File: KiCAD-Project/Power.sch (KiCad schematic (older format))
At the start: 19 parts, among them U401 DRV8323SRTAR-DRV8323SRTAR

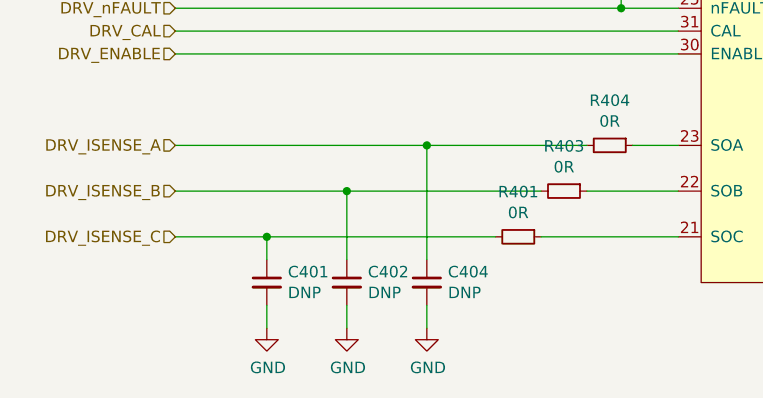
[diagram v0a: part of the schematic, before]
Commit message: Schamtic package assigned
Package assigned, added two 100nF C's for temp sensors
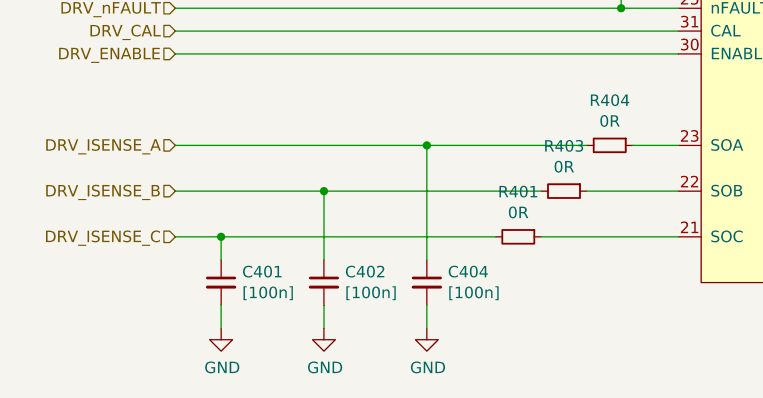
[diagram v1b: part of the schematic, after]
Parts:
- C401, C402, C404: value DNP -> [100n]; footprint (none) -> Capacitor_SMD:C_0603_1608Metric
- C403: footprint (none) -> Capacitor_SMD:C_1206_3216Metric
- C405, C406, C407, C408, C409: footprint (none) -> Capacitor_SMD:C_0603_1608Metric
- R401, R402, R403, R404, R405: footprint (none) -> Resistor_SMD:R_0603_1608Metric
- TP401, TP402, TP403, TP404: footprint (none) -> TestPoint:TestPoint_Pad_D2.0mm
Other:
- moved on the sheet: C401, C402
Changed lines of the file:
@@
 F 0 "R405" H 5009 4096 50  0000 L CNN
 F 1 "10k" H 5009 4005 50  0000 L CNN
-F 2 "" H 4950 4050 50  0001 C CNN
+F 2 "Resistor_SMD:R_0603_1608Metric" H 4950 4050 50  0001 C CNN
 F 3 "~" H 4950 4050 50  0001 C CNN
 	1    4950 4050
@@
 F 0 "R402" H 4709 4096 50  0000 L CNN
 F 1 "10k" H 4709 4005 50  0000 L CNN
-F 2 "" H 4650 4050 50  0001 C CNN
+F 2 "Resistor_SMD:R_0603_1608Metric" H 4650 4050 50  0001 C CNN
 F 3 "~" H 4650 4050 50  0001 C CNN
 	1    4650 4050
@@
 F 0 "R404" V 4704 5200 50  0000 C CNN
 F 1 "0R" V 4795 5200 50  0000 C CNN
-F 2 "" H 4900 5200 50  0001 C CNN
+F 2 "Resistor_SMD:R_0603_1608Metric" H 4900 5200 50  0001 C CNN
 F 3 "~" H 4900 5200 50  0001 C CNN
 	1    4900 5200
@@
 F 0 "R403" V 4504 5400 50  0000 C CNN
 F 1 "0R" V 4595 5400 50  0000 C CNN
-F 2 "" H 4700 5400 50  0001 C CNN
+F 2 "Resistor_SMD:R_0603_1608Metric" H 4700 5400 50  0001 C CNN
 F 3 "~" H 4700 5400 50  0001 C CNN
 	1    4700 5400
@@
 F 0 "R401" V 4304 5600 50  0000 C CNN
 F 1 "0R" V 4395 5600 50  0000 C CNN
-F 2 "" H 4500 5600 50  0001 C CNN
+F 2 "Resistor_SMD:R_0603_1608Metric" H 4500 5600 50  0001 C CNN
 F 3 "~" H 4500 5600 50  0001 C CNN
 	1    4500 5600
@@
 AR Path="/60AFCC9B/60B2332E" Ref="C404"  Part="1"
 F 0 "C404" H 4192 5846 50  0000 L CNN
-F 1 "DNP" H 4192 5755 50  0000 L CNN
-F 2 "" H 4100 5800 50  0001 C CNN
+F 1 "[100n]" H 4192 5755 50  0000 L CNN
+F 2 "Capacitor_SMD:C_0603_1608Metric" H 4100 5800 50  0001 C CNN
 F 3 "~" H 4100 5800 50  0001 C CNN
 	1    4100 5800
@@
 F 0 "TP403" H 3858 4218 50  0000 L CNN
 F 1 "SPI_SCK" H 3858 4127 50  0000 L CNN
-F 2 "" H 4000 4100 50  0001 C CNN
+F 2 "TestPoint:TestPoint_Pad_D2.0mm" H 4000 4100 50  0001 C CNN
 F 3 "~" H 4000 4100 50  0001 C CNN
 	1    3800 4100
@@
 F 0 "TP401" H 3258 4218 50  0000 L CNN
 F 1 "MOSI" H 3258 4127 50  0000 L CNN
-F 2 "" H 3400 4100 50  0001 C CNN
+F 2 "TestPoint:TestPoint_Pad_D2.0mm" H 3400 4100 50  0001 C CNN
 F 3 "~" H 3400 4100 50  0001 C CNN
 	1    3200 4100
@@
 F 0 "TP402" H 3558 4218 50  0000 L CNN
 F 1 "MISO" H 3558 4127 50  0000 L CNN
-F 2 "" H 3700 4100 50  0001 C CNN
+F 2 "TestPoint:TestPoint_Pad_D2.0mm" H 3700 4100 50  0001 C CNN
 F 3 "~" H 3700 4100 50  0001 C CNN
 	1    3500 4100
@@
 F 0 "TP404" H 4258 4218 50  0000 L CNN
 F 1 "DRV_CS" H 4258 4127 50  0000 L CNN
-F 2 "" H 4400 4100 50  0001 C CNN
+F 2 "TestPoint:TestPoint_Pad_D2.0mm" H 4400 4100 50  0001 C CNN
 F 3 "~" H 4400 4100 50  0001 C CNN
 	1    4200 4100
@@
 F 0 "C408" H 4942 1696 50  0000 L CNN
 F 1 "1u" H 4942 1605 50  0000 L CNN
-F 2 "" H 4850 1650 50  0001 C CNN
+F 2 "Capacitor_SMD:C_0603_1608Metric" H 4850 1650 50  0001 C CNN
 F 3 "~" H 4850 1650 50  0001 C CNN
 	1    4850 1650
@@
 F 0 "C409" H 4942 2146 50  0000 L CNN
 F 1 "47n" H 4942 2055 50  0000 L CNN
-F 2 "" H 4850 2100 50  0001 C CNN
+F 2 "Capacitor_SMD:C_0603_1608Metric" H 4850 2100 50  0001 C CNN
 F 3 "~" H 4850 2100 50  0001 C CNN
 	1    4850 2100
@@
 F 0 "C405" H 4492 1696 50  0000 L CNN
 F 1 "100n" H 4492 1605 50  0000 L CNN
-F 2 "" H 4400 1650 50  0001 C CNN
+F 2 "Capacitor_SMD:C_0603_1608Metric" H 4400 1650 50  0001 C CNN
 F 3 "~" H 4400 1650 50  0001 C CNN
 	1    4400 1650
@@
 F 0 "C403" H 4192 1696 50  0000 L CNN
 F 1 "10u" H 4192 1605 50  0000 L CNN
-F 2 "" H 4100 1650 50  0001 C CNN
+F 2 "Capacitor_SMD:C_1206_3216Metric" H 4100 1650 50  0001 C CNN
 F 3 "~" H 4100 1650 50  0001 C CNN
 	1    4100 1650
@@
 F 0 "C406" H 4492 2696 50  0000 L CNN
 F 1 "1u" H 4492 2605 50  0000 L CNN
-F 2 "" H 4400 2650 50  0001 C CNN
+F 2 "Capacitor_SMD:C_0603_1608Metric" H 4400 2650 50  0001 C CNN
 F 3 "~" H 4400 2650 50  0001 C CNN
 	1    4400 2650
@@
 F 0 "C407" H 4792 2696 50  0000 L CNN
 F 1 "100n" H 4792 2605 50  0000 L CNN
-F 2 "" H 4700 2650 50  0001 C CNN
+F 2 "Capacitor_SMD:C_0603_1608Metric" H 4700 2650 50  0001 C CNN
 F 3 "~" H 4700 2650 50  0001 C CNN
 	1    4700 2650
@@
 L Device:C_Small C?
 U 1 1 617E419E
-P 3750 5800
+P 3650 5800
 AR Path="/617E419E" Ref="C?"  Part="1"
 AR Path="/60AFCC9B/617E419E" Ref="C402"  Part="1"
-F 0 "C402" H 3842 5846 50  0000 L CNN
-F 1 "DNP" H 3842 5755 50  0000 L CNN
-F 2 "" H 3750 5800 50  0001 C CNN
-F 3 "~" H 3750 5800 50  0001 C CNN
-	1    3750 5800
+F 0 "C402" H 3742 5846 50  0000 L CNN
+F 1 "[100n]" H 3742 5755 50  0000 L CNN
+F 2 "Capacitor_SMD:C_0603_1608Metric" H 3650 5800 50  0001 C CNN
+F 3 "~" H 3650 5800 50  0001 C CNN
+	1    3650 5800
 	1    0    0    -1
 $EndComp
@@
 L Device:C_Small C?
 U 1 1 617EB3D4
-P 3400 5800
+P 3200 5800
 AR Path="/617EB3D4" Ref="C?"  Part="1"
 AR Path="/60AFCC9B/617EB3D4" Ref="C401"  Part="1"
-F 0 "C401" H 3492 5846 50  0000 L CNN
-F 1 "DNP" H 3492 5755 50  0000 L CNN
-F 2 "" H 3400 5800 50  0001 C CNN
-F 3 "~" H 3400 5800 50  0001 C CNN
-	1    3400 5800
+F 0 "C401" H 3292 5846 50  0000 L CNN
+F 1 "[100n]" H 3292 5755 50  0000 L CNN
+F 2 "Capacitor_SMD:C_0603_1608Metric" H 3200 5800 50  0001 C CNN
+F 3 "~" H 3200 5800 50  0001 C CNN
+	1    3200 5800
 	1    0    0    -1
 $EndComp
@@
 L power:GND #PWR?
 U 1 1 617EB72F
-P 3400 6000
+P 3200 6000
 AR Path="/617EB72F" Ref="#PWR?"  Part="1"
 AR Path="/60AFCC9B/617EB72F" Ref="#PWR0401"  Part="1"
-F 0 "#PWR0401" H 3400 5750 50  0001 C CNN
-F 1 "GND" H 3405 5827 50  0000 C CNN
-F 2 "" H 3400 6000 50  0001 C CNN
-F 3 "" H 3400 6000 50  0001 C CNN
-	1    3400 6000
+F 0 "#PWR0401" H 3200 5750 50  0001 C CNN
+F 1 "GND" H 3205 5827 50  0000 C CNN
+F 2 "" H 3200 6000 50  0001 C CNN
+F 3 "" H 3200 6000 50  0001 C CNN
+	1    3200 6000
 	1    0    0    -1
 $EndComp
@@
 L power:GND #PWR?
 U 1 1 617EC2F0
-P 3750 6000
+P 3650 6000
 AR Path="/617EC2F0" Ref="#PWR?"  Part="1"
 AR Path="/60AFCC9B/617EC2F0" Ref="#PWR0402"  Part="1"
-F 0 "#PWR0402" H 3750 5750 50  0001 C CNN
-F 1 "GND" H 3755 5827 50  0000 C CNN
-F 2 "" H 3750 6000 50  0001 C CNN
-F 3 "" H 3750 6000 50  0001 C CNN
-	1    3750 6000
+F 0 "#PWR0402" H 3650 5750 50  0001 C CNN
+F 1 "GND" H 3655 5827 50  0000 C CNN
+F 2 "" H 3650 6000 50  0001 C CNN
+F 3 "" H 3650 6000 50  0001 C CNN
+	1    3650 6000
 	1    0    0    -1
 $EndComp
@@
 $EndComp
 Wire Wire Line
-	3400 6000 3400 5900
-Wire Wire Line
-	3750 5900 3750 6000
+	3200 6000 3200 5900
+Wire Wire Line
+	3650 5900 3650 6000
 Wire Wire Line
 	4100 6000 4100 5900
@@
 	4100 5200 4800 5200
 Wire Wire Line
-	3400 5700 3400 5600
-Wire Wire Line
-	3400 5600 4400 5600
-Wire Wire Line
-	3750 5700 3750 5400
-Wire Wire Line
-	3750 5400 4600 5400
-Wire Wire Line
-	3750 5400 3000 5400
-Connection ~ 3750 5400
-Wire Wire Line
-	3400 5600 3000 5600
-Connection ~ 3400 5600
+	3200 5700 3200 5600
+Wire Wire Line
+	3650 5700 3650 5400
 Wire Wire Line
 	3000 5200 4100 5200
@@
 Wire Wire Line
 	4200 4500 5200 4500
+Connection ~ 3200 5600
+Wire Wire Line
+	3200 5600 3000 5600
+Wire Wire Line
+	3200 5600 4400 5600
+Connection ~ 3650 5400
+Wire Wire Line
+	3650 5400 3000 5400
+Wire Wire Line
+	3650 5400 4600 5400
 $EndSCHEMATC

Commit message: pcb draft
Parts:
- U401: footprint Package_DFN_QFN:VQFN-48-1EP_7x7mm_P0.5mm_EP5.15x5.15mm_ThermalVias -> Package_DFN_QFN:Texas_S-PVQFN-N40_EP4.15x4.15mm_ThermalVias
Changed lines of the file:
@@
 F 0 "U401" H 6300 1565 50  0000 C CNN
 F 1 "DRV8323SRTAR-DRV8323SRTAR" H 6300 1474 50  0000 C CNN
-F 2 "Package_DFN_QFN:VQFN-48-1EP_7x7mm_P0.5mm_EP5.15x5.15mm_ThermalVias" H 6150 1600 50  0001 C CNN
+F 2 "Package_DFN_QFN:Texas_S-PVQFN-N40_EP4.15x4.15mm_ThermalVias" H 6150 1600 50  0001 C CNN
 F 3 "" H 6150 1600 50  0001 C CNN
 	1    5300 1400
 	1    0    0    -1
 $EndComp
-Wire Wire Line
-	4850 2000 5200 2000
 Wire Wire Line
 	4850 2200 5200 2200
@@
 $EndComp
 Wire Wire Line
-	5200 2400 4700 2400
-Wire Wire Line
 	4700 2400 4700 2550
 Wire Wire Line
@@
 Wire Wire Line
 	3650 5400 4600 5400
+Wire Wire Line
+	4850 2000 5200 2000
+Wire Wire Line
+	5200 2400 4700 2400
 $EndSCHEMATC

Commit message: layout redesign started
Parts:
- C403: footprint Capacitor_SMD:C_1206_3216Metric -> Capacitor_SMD:C_0603_1608Metric
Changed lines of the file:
@@
 F 0 "C403" H 4192 1696 50  0000 L CNN
 F 1 "10u" H 4192 1605 50  0000 L CNN
-F 2 "Capacitor_SMD:C_1206_3216Metric" H 4100 1650 50  0001 C CNN
+F 2 "Capacitor_SMD:C_0603_1608Metric" H 4100 1650 50  0001 C CNN
 F 3 "~" H 4100 1650 50  0001 C CNN
 	1    4100 1650
